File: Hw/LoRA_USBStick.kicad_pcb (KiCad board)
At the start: 2 copper layers, 61.5 x 18.7 mm, 36 parts, among them J10 USB_B, J4 SWD, SW3 RST, U1 RP2040, U2 RFM95W-868S2, U3 AP2112K-3.3, U4 W25Q16JV, Y1 12Mhz

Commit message: PCB route
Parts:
- removed J4: SWD, Connector:Tag-Connect_TC2030-IDC-NL_2x03_P1.27mm_Vertical
- moved SW3 24.7 mm to (151.2, 109.2), turned to -90 degrees
- moved C16 19.8 mm to (132.1, 106.6), turned to 90 degrees
- moved C13 15.4 mm to (135.1, 106.6), turned to 90 degrees
- moved C12 14.3 mm to (137.0, 106.5), turned to 90 degrees
- moved C9 14.0 mm to (133.6, 106.6), turned to 90 degrees
- moved C11 13.9 mm to (139.3, 106.5), turned to 90 degrees
- moved C10 12.9 mm to (149.7, 115.7), turned to 0 degrees
- moved D2 11.6 mm to (131.2, 122.4)
- moved C17 10.6 mm to (127.2, 118.0), turned to -90 degrees
- moved C4 10.00 mm to (131.8, 112.5), turned to 180 degrees
- moved C2 9.84 mm to (149.7, 114.2), turned to 0 degrees
- moved R11 9.68 mm to (142.3, 105.8), turned to 0 degrees
- moved R9 9.63 mm to (135.9, 122.5), turned to 180 degrees
- moved R5 8.73 mm to (127.2, 120.7), turned to 0 degrees
- moved C8 8.04 mm to (131.8, 111.1), turned to 180 degrees
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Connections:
- R11 pad 1: /Rx_LED -> /RX_LED
- U1 pad 2: /RX_LED -> unconnected-(U1-Pad2)
- U1 pad 24: /SWCLK -> unconnected-(U1-Pad24)
- U1 pad 25: /SWDIO -> unconnected-(U1-Pad25)
- U1 pad 37: unconnected-(U1-Pad37) -> /RX_LED
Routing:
- net +3V3: track 0.00 -> 139.6 mm, vias 0 -> 10
- net +1V2: track 0.00 -> 40.7 mm, vias 0 -> 4
- net /RFM_RST: track 0.00 -> 39.4 mm, vias 0 -> 2
- net /SCK: track 0.00 -> 34.5 mm, vias 0 -> 2
- net GND: track 0.00 -> 34.1 mm, vias 0 -> 8
- net /SS: track 0.00 -> 33.6 mm, vias 0 -> 2
- net /MOSI: track 0.00 -> 33.2 mm, vias 0 -> 2
- net /DIO5: track 0.00 -> 31.3 mm, vias 0 -> 2
- net /DIO0: track 0.00 -> 30.9 mm, vias 0 -> 2
- net /DIO1: track 0.00 -> 27.1 mm, vias 0 -> 2
- net /MISO: track 0.00 -> 25.3 mm, vias 0 -> 2
- net /DIO2: track 0.00 -> 23.9 mm, vias 0 -> 2
- net VBUS: track 0.00 -> 19.1 mm, vias 0 -> 3
- net /QSPI_CS: track 0.00 -> 17.9 mm, vias 0 -> 2
- net /RD-: track 0.00 -> 17.4 mm, vias 0 -> 2
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
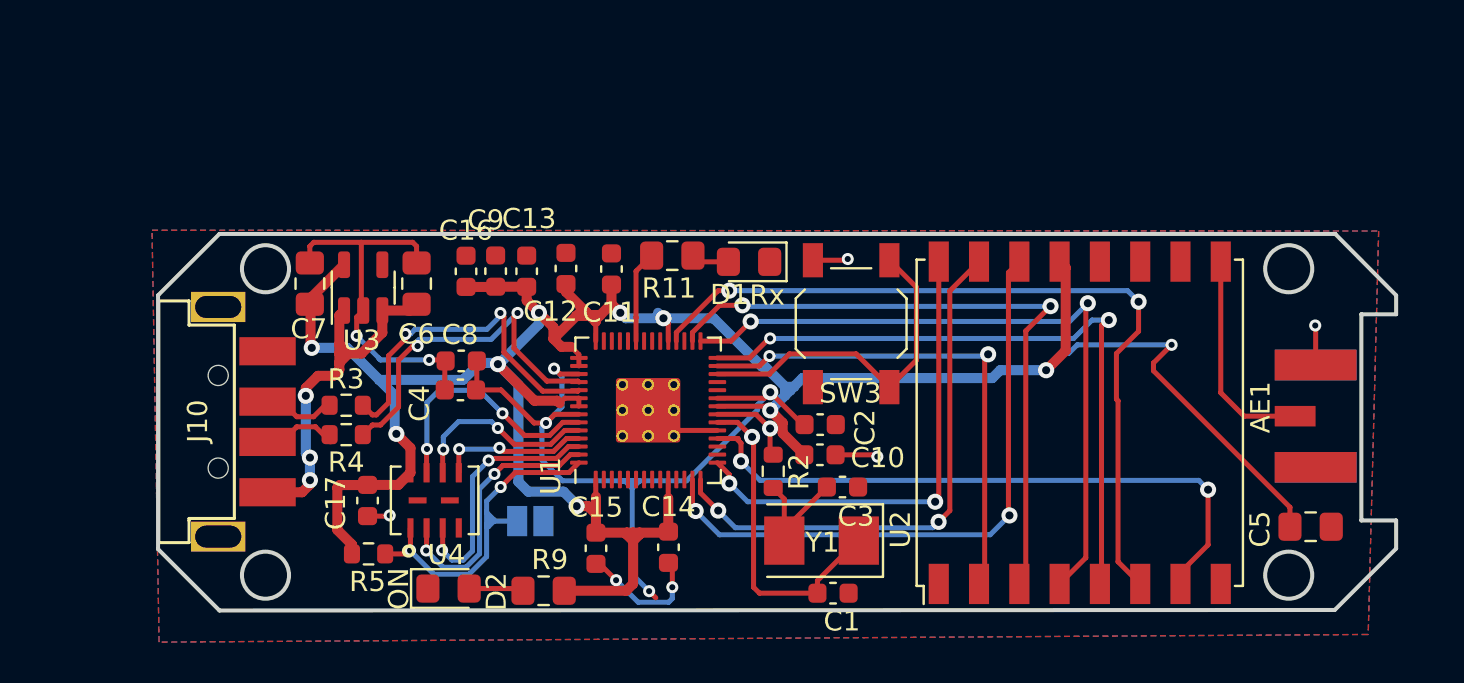
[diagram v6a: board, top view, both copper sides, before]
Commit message: update floorplan and routing
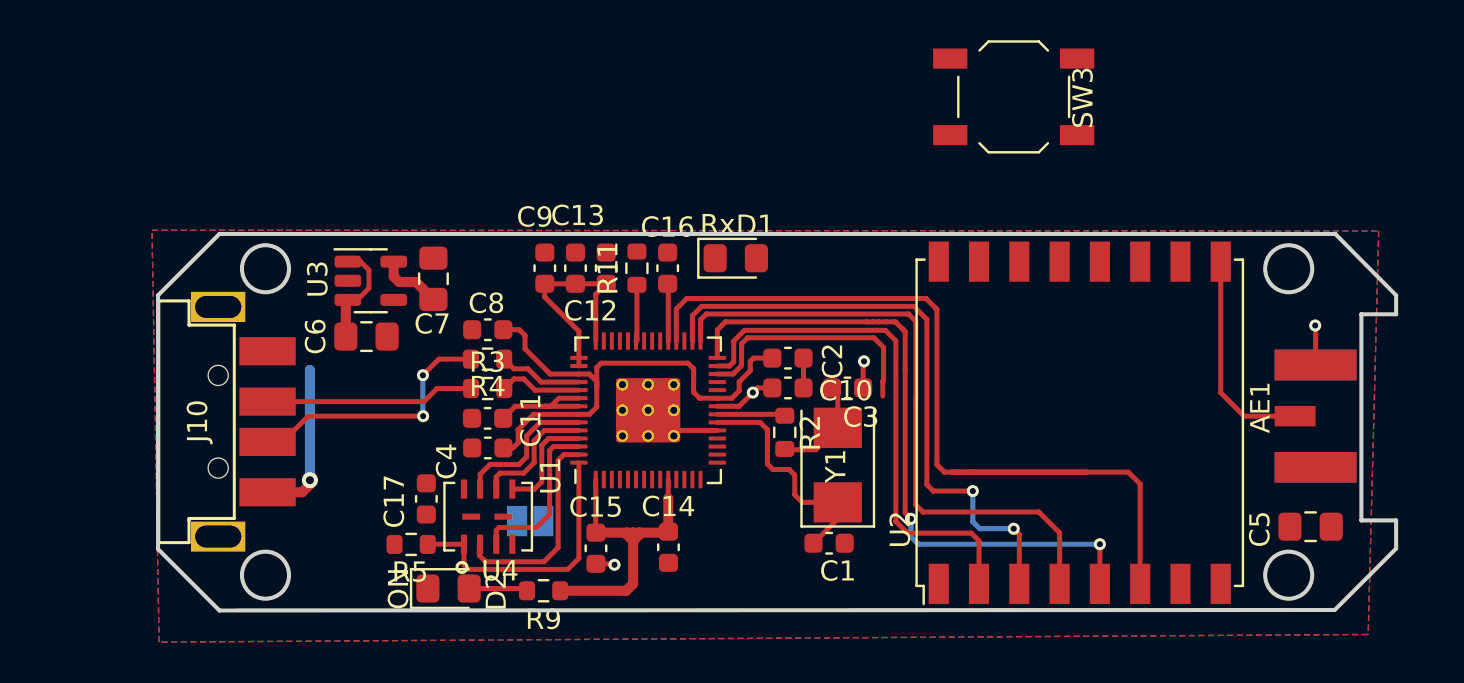
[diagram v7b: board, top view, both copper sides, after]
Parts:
- R11, R9: footprint Resistor_SMD:R_0805_2012Metric_Pad1.15x1.40mm_HandSolder -> Resistor_SMD:R_0603_1608Metric
- moved SW3 13.9 mm to (159.3, 98.0), turned to 0 degrees
- moved C16 10.0 mm to (142.1, 106.5)
- moved C11 9.63 mm to (133.2, 113.9), turned to 180 degrees
- moved R4 7.96 mm to (133.2, 111.0)
- moved R3 7.07 mm to (133.2, 112.5)
- moved C7 6.14 mm to (130.5, 107.0)
- moved C3 4.93 mm to (151.0, 112.4)
- moved Y1 3.84 mm to (150.5, 116.2), turned to 90 degrees
- moved C10 3.68 mm to (148.1, 112.4)
- moved C2 3.67 mm to (148.1, 110.9)
- moved C6 3.62 mm to (127.1, 109.9), turned to 0 degrees
- moved C4 3.18 mm to (133.2, 115.4)
- moved C17 2.92 mm to (130.1, 117.9)
- moved U4 2.78 mm to (133.2, 118.8)
- moved C1 2.49 mm to (150.1, 120.1)
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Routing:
- net +3V3: track 139.6 -> 42.0 mm, vias 10 -> 1
- net /DIO5: track 31.3 -> 0.00 mm, vias 2 -> 0
- net /DIO0: track 30.9 -> 0.00 mm, vias 2 -> 0
- net /DIO1: track 27.1 -> 0.00 mm, vias 2 -> 0
- net GND: track 34.1 -> 8.00 mm, vias 8 -> 3
- net /DIO2: track 23.9 -> 0.00 mm, vias 2 -> 0
- net +1V2: track 40.7 -> 25.7 mm, vias 4 -> 0
- net /RD-: track 17.4 -> 4.18 mm, vias 2 -> 0
- net /RD+: track 17.3 -> 4.13 mm, vias 2 -> 0
- net /D-: track 3.75 -> 13.0 mm, vias 0 -> 2
- net /D+: track 3.66 -> 10.4 mm
- net VBUS: track 19.1 -> 13.2 mm, vias 3 -> 1
- net /RFM_RST: track 39.4 -> 44.8 mm, vias 2 -> 0
- net /QSPI_DATA3: track 12.5 -> 7.31 mm, vias 2 -> 0
- net /RST: track 17.1 -> 12.3 mm
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
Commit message: Change a fototprint and routing
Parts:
- SW3: footprint Button_Switch_SMD:SW_SPST_TL3342 -> Switches:C455281
- moved C5 25.2 mm to (152.4, 106.3), turned to 180 degrees
- moved SW3 22.4 mm to (148.1, 117.4), turned to -90 degrees
- moved C16 1.46 mm to (142.1, 107.9)
- moved C12 1.44 mm to (139.0, 107.9)
- moved Y1 0.41 mm to (150.6, 116.7)
- moved C1 0.37 mm to (150.2, 120.5)
- moved R2 0.37 mm to (147.9, 115.0)
- moved C2 0.36 mm to (148.1, 111.3)
- moved C10 0.35 mm to (148.1, 112.8)
- moved C3 0.35 mm to (151.0, 112.8)
- moved R11 0.32 mm to (140.5, 106.8)
- turned D1 to 180 degrees
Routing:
- net +3V3: track 42.0 -> 107.7 mm, vias 1 -> 11
- net /DIO5: track 0.00 -> 42.5 mm, vias 0 -> 2
- net /DIO0: track 0.00 -> 36.2 mm, vias 0 -> 2
- net /DIO1: track 0.00 -> 32.3 mm, vias 0 -> 2
- net /DIO2: track 0.00 -> 30.7 mm, vias 0 -> 2
- net /RST: track 12.3 -> 29.0 mm
- net GND: track 8.00 -> 24.5 mm, vias 3 -> 14
- net /RFM_RST: track 44.8 -> 34.9 mm
- net /QSPI_CS: track 13.6 -> 17.8 mm, vias 0 -> 1
- net Net-(D1-Pad2): track 0.00 -> 3.92 mm
- net VBUS: track 13.2 -> 16.3 mm, vias 1 -> 2
- net /SS: track 32.9 -> 30.9 mm
- net /SCK: track 31.4 -> 29.5 mm
- net /MOSI: track 30.5 -> 29.6 mm
- net /MISO: track 26.0 -> 25.2 mm
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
